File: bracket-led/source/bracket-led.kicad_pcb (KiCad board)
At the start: 2 copper layers, 37 x 11 mm, 6 parts, among them J1 SM08B-SURS-TF(LF)(SN)

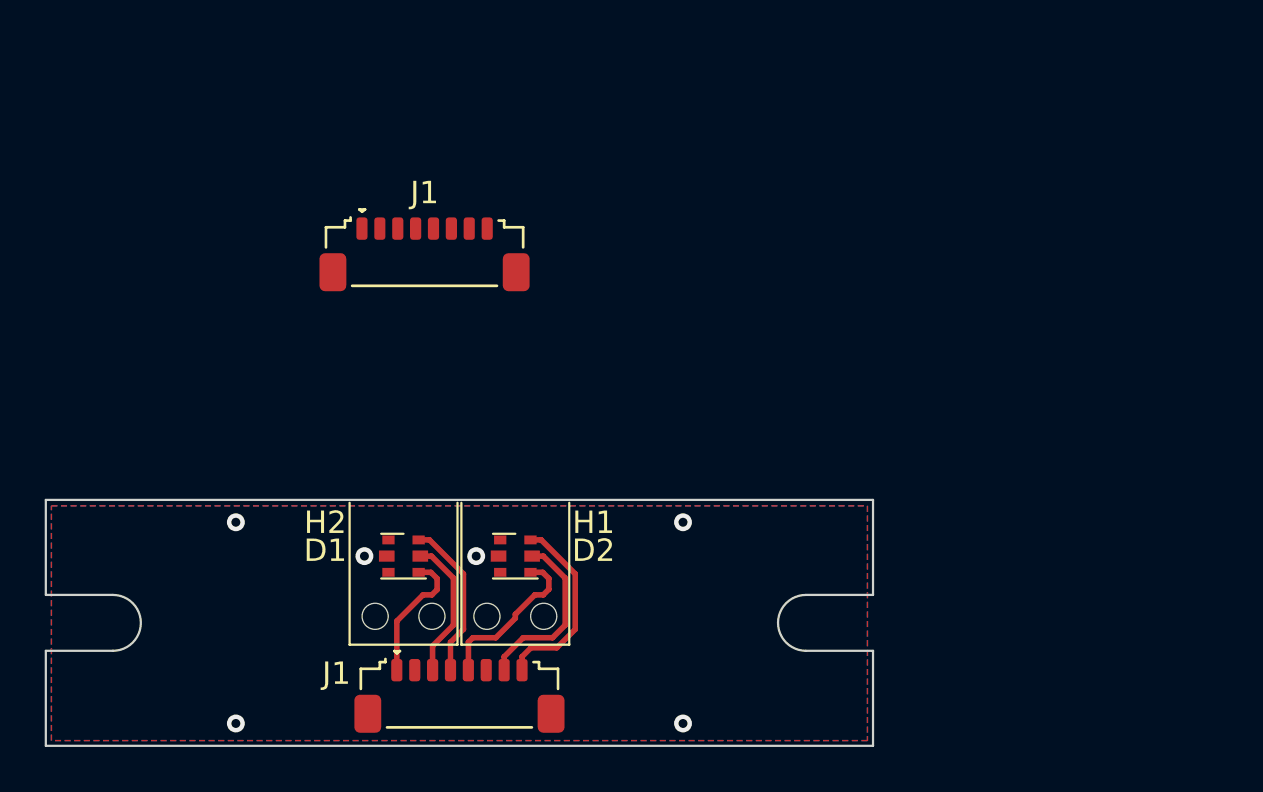
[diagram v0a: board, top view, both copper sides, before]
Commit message: fixed pcb led-connector mapping
be warned that schematic does not match pcb in an effort to get this to filipe for order asap
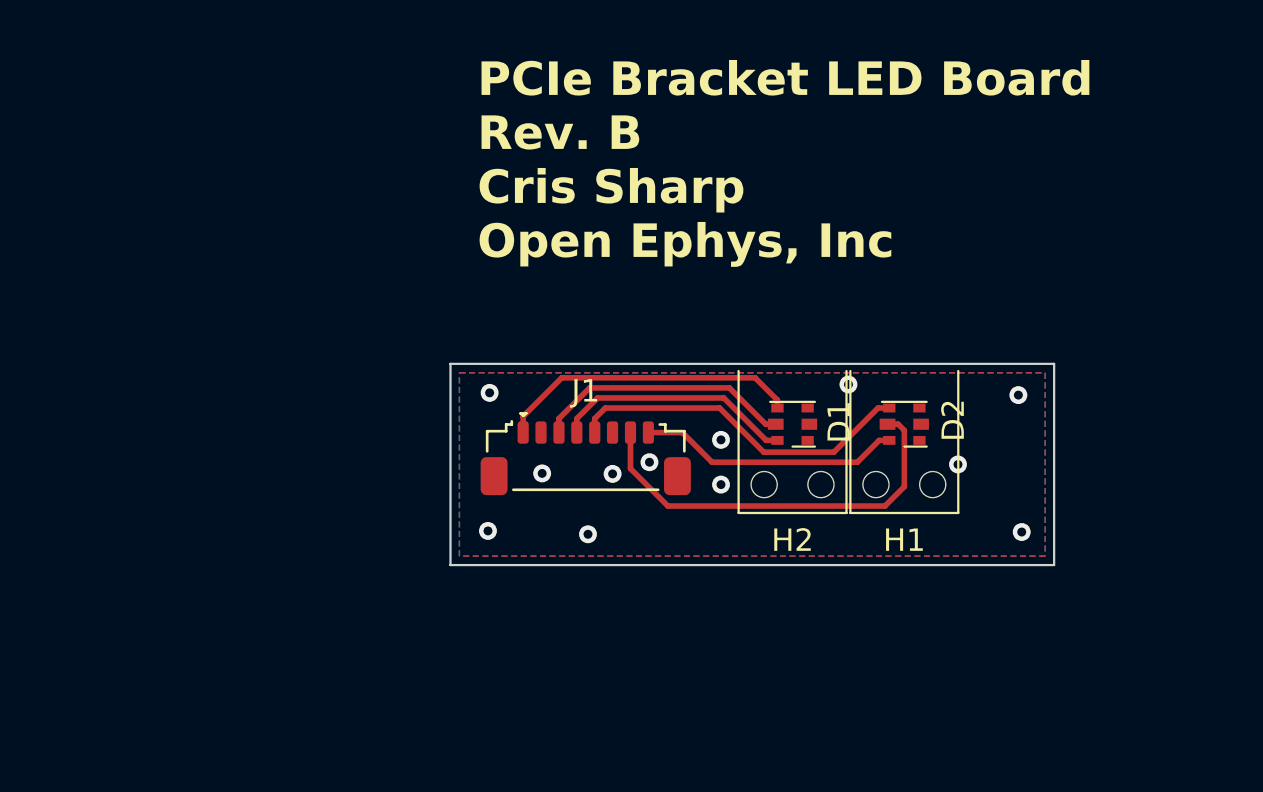
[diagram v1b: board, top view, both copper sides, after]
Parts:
- removed the J1 at (50.0, 56.2)
- removed the J1 at (48.4, 36.5)
- added J1: SM08B-SURS-TF(LF)(SN), Open Ephys:JST_SM08B-SURS-TF(LF)(SN), F.Cu at (55.7, 45.6)
- moved D1 18.4 mm to (64.9, 44.1), turned to 180 degrees
- moved D2 18.4 mm to (69.9, 44.1), turned to 180 degrees
- moved H1 18.4 mm to (69.9, 46.8)
- moved H2 18.4 mm to (64.9, 46.8)
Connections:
- D1 pad 1: /B_{B} -> B_{B}
- D1 pad 3: /R_{B} -> R_{B}
- D1 pad 5: /G_{B} -> G_{B}
- D2 pad 1: /B_{A} -> B_{A}
- D2 pad 3: /R_{A} -> R_{A}
- D2 pad 5: /G_{A} -> G_{A}
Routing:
- net R_{A}: track 0.00 -> 18.3 mm
- net G_{A}: track 0.00 -> 15.6 mm
- net G_{B}: track 0.00 -> 13.6 mm
- net B_{A}: track 0.00 -> 11.7 mm
- net R_{B}: track 0.00 -> 11.6 mm
- net B_{B}: track 0.00 -> 10.8 mm
- net /B2: track 8.85 -> 0.00 mm
- net /R2: track 8.16 -> 0.00 mm
- net /G2: track 7.60 -> 0.00 mm
- net /B1: track 7.43 -> 0.00 mm
- net /R1: track 6.64 -> 0.00 mm
- net /G1: track 6.27 -> 0.00 mm
- net GND: vias 6 -> 12
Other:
- board size 37 x 11 mm -> 27 x 9 mm
- board text added: "LED_RGB"
- board text added: "PCIe Bracket LED Board Rev. B Cris Sharp Open Ephys, Inc"
- board text added: "Rev. B"
- board text added: "SM08B-SURS-TF(LF)(SN)"
- board text removed: "#2 or M2 SHCS screw fit in slots"
- board text removed: "Rev. A"
